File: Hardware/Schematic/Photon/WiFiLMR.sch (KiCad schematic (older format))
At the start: 0 parts

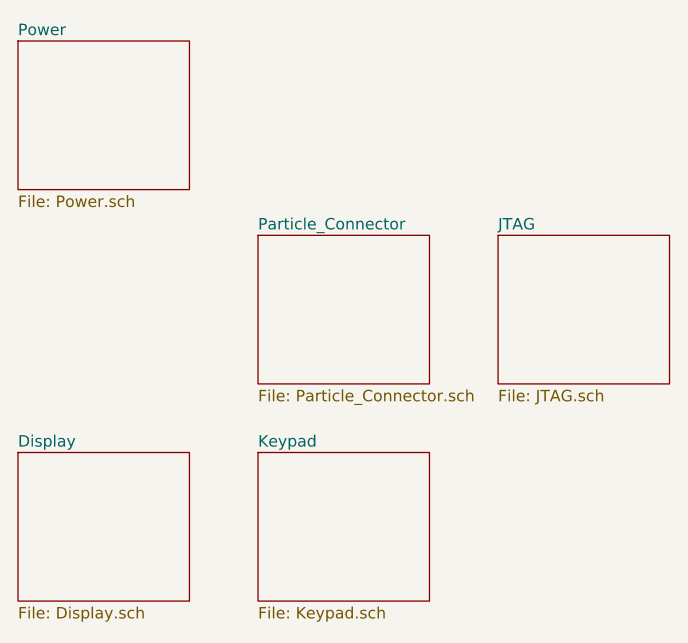
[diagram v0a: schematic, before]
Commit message: Split-up schematics into three seperate projects with a parts library as well
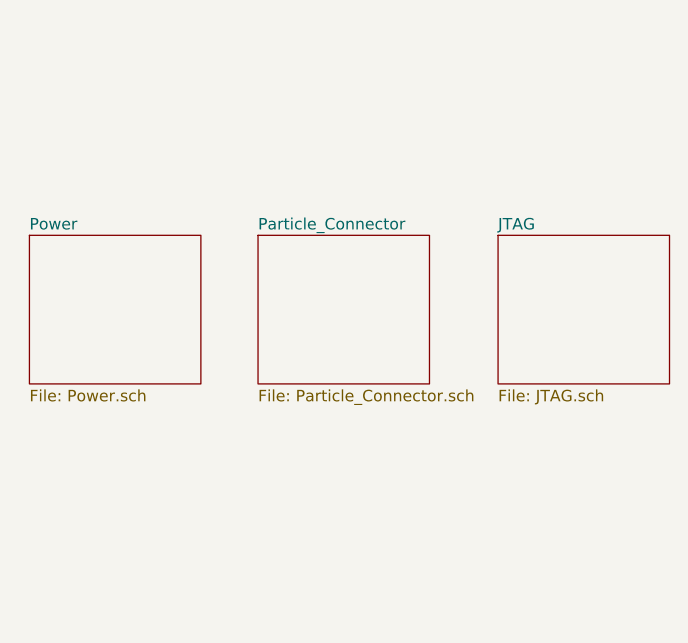
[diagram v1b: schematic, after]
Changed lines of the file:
@@
 $Descr A4 11693 8268
 encoding utf-8
-Sheet 1 6
+Sheet 1 5
 Title ""
 Date ""
@@
 $EndSheet
 $Sheet
-S 5850 3950 750  650
-U 5D1772AD
-F0 "Keypad" 50
-F1 "Keypad.sch" 50
-$EndSheet
-$Sheet
-S 4800 3950 750  650
-U 5D193223
-F0 "Display" 50
-F1 "Display.sch" 50
-$EndSheet
-$Sheet
-S 4800 2150 750  650
+S 4850 3000 750  650
 U 5D21B5D5
 F0 "Power" 50
